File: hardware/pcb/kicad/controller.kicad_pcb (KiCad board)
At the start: 6 copper layers, 160 x 130 mm, 29 parts, among them J1 48V_INPUT_10A, J10 ESTOP_RED_KEYED_DUAL_CHANNEL, J11 SAFETY_GATE_OUTPUT, J2 12V_OUTPUT_16A, J3 JETSON_DEVKIT_12V_5A, J4 JETSON_MCU_BACKPLANE, J5 CAN_A, J6 CAN_B, U1 LM5069_HOTSWAP, U2 DCM3623_48V_12V_240W, U3 JETSON_12V_EFUSE_5A, U4 BUCK_12V_3V3_5A, U5 CH32V307_CARRIER, U6 ISO1042DW, U7 3V3_5V_ISOLATED_DC_DC, U8 DUAL_CHANNEL_SAFETY_GATE_CARR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

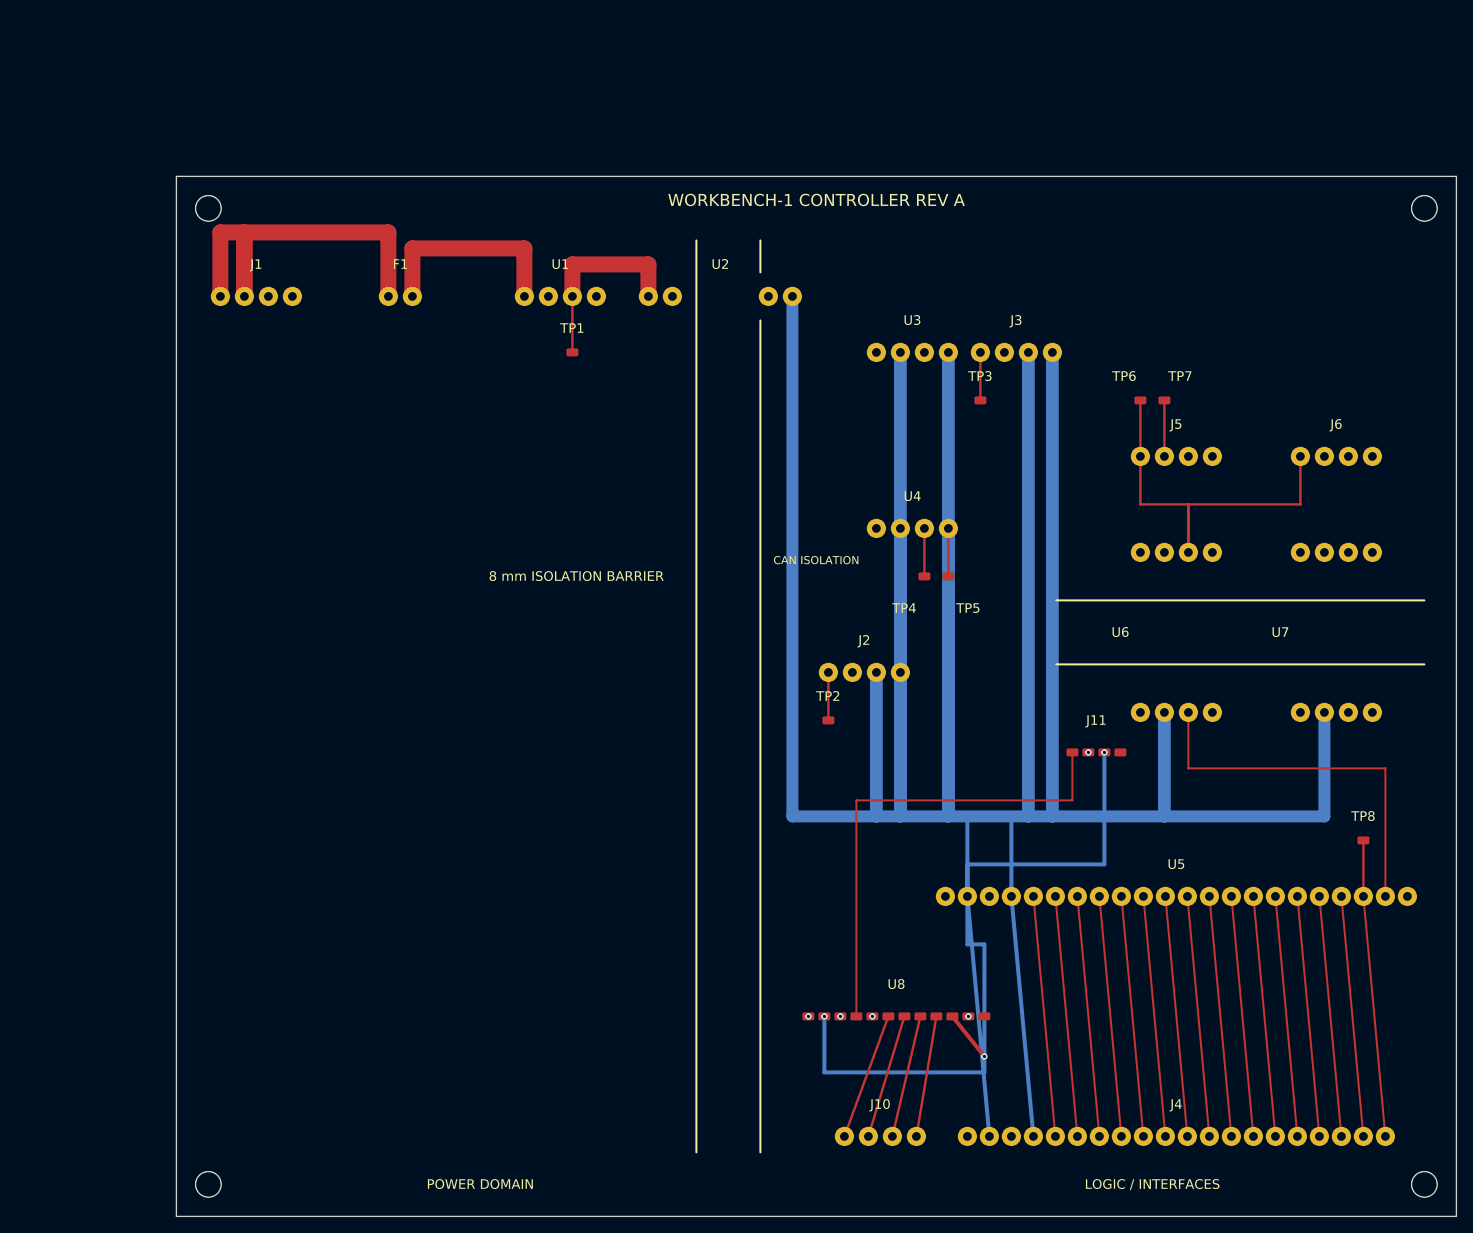
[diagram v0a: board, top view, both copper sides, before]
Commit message: feat(hardware): integrate eight-layer chassis traction package
Add reproducible eight-layer controller schematic/layout and fabrication outputs, plus fail-closed traction childboard, wheel, battery, and chassis envelopes. Keep motor, AVL, safety, supplier, and physical validation gates blocked until external evidence is attached.
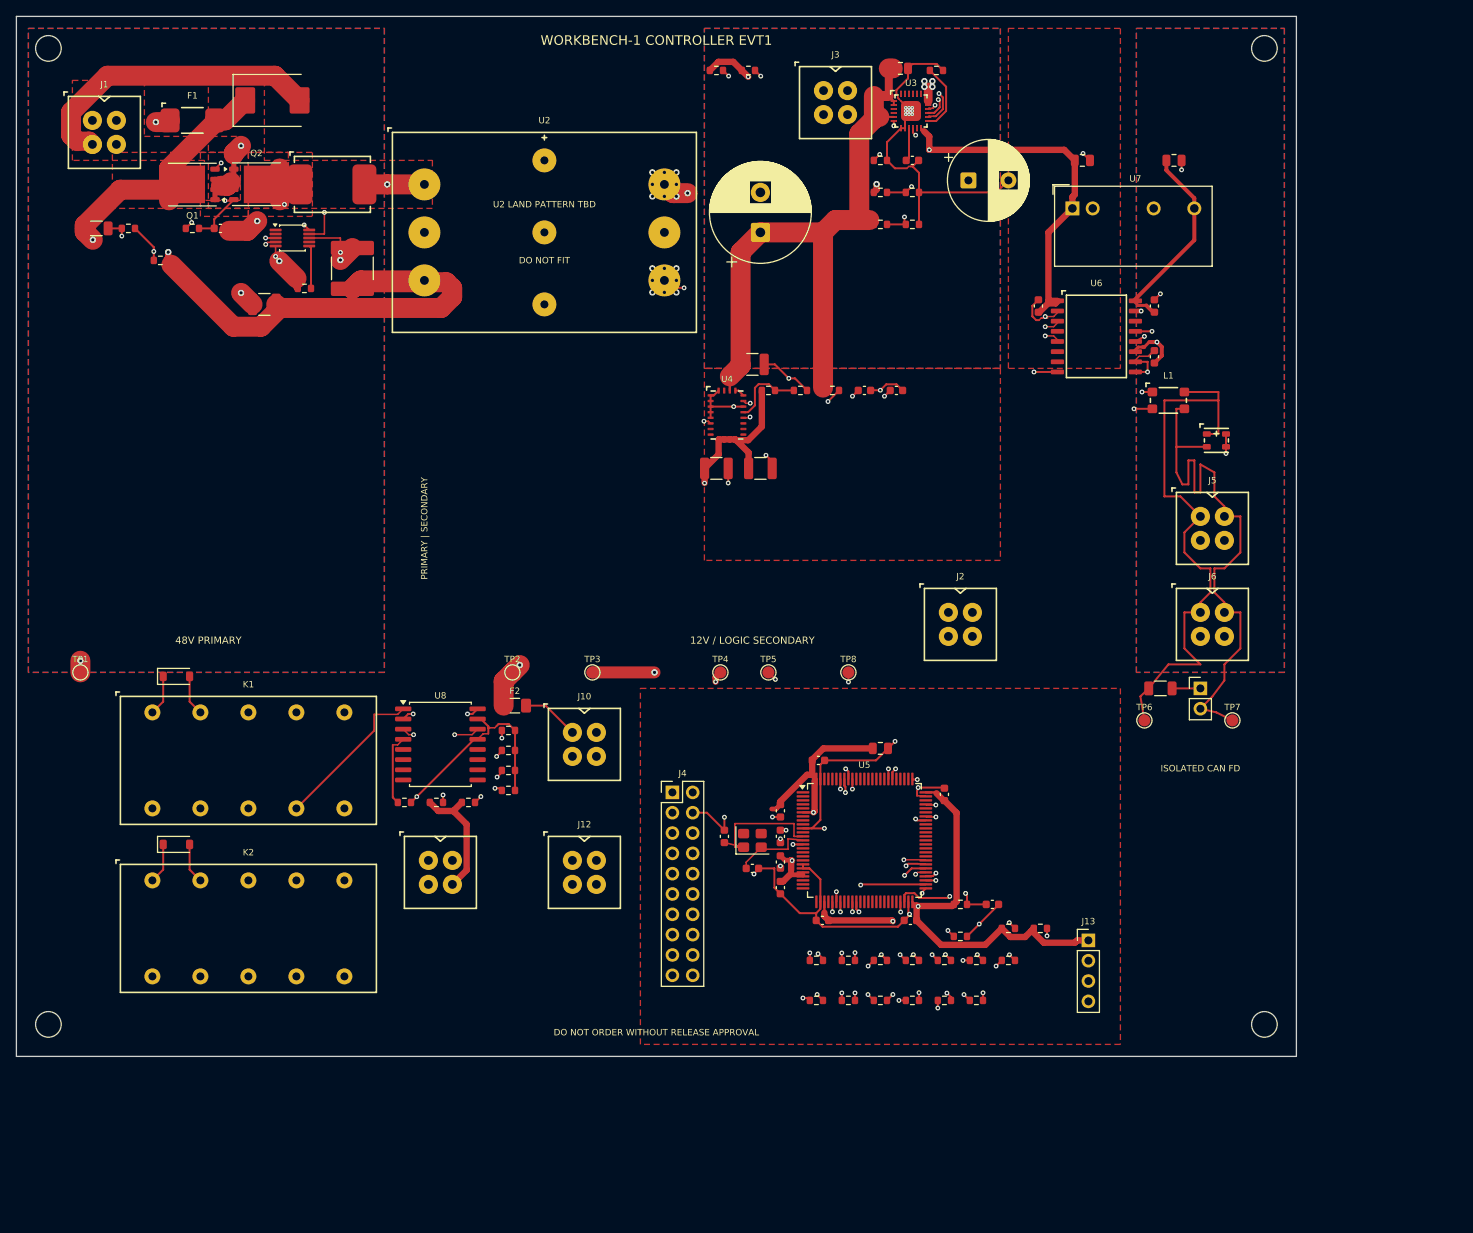
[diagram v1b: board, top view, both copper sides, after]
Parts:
- added C1: 1uF 100V, C_1210_3225Metric, F.Cu at (31.0, 36.0)
- added C10: 100nF, C_0603_1608Metric, F.Cu at (95.5, 102.5)
- added C11: 100nF, C_0603_1608Metric, F.Cu at (95.5, 105.7)
- added C12: 100nF, C_0603_1608Metric, F.Cu at (95.5, 108.9)
- added C13: 100nF, C_0603_1608Metric, F.Cu at (100.8, 113.0)
- added C14: 100nF, C_0603_1608Metric, F.Cu at (111.8, 113.0)
- added C15: 100nF, C_0603_1608Metric, F.Cu at (116.0, 97.2)
- added C16: 100nF, C_0603_1608Metric, F.Cu at (100.2, 93.0)
- added C17: 4.7uF, C_0805_2012Metric, F.Cu at (108.0, 91.5)
- added C18: 100nF, C_0603_1608Metric, F.Cu at (112.0, 18.0)
- added C19: 100nF, C_0603_1608Metric, F.Cu at (122.0, 111.0)
- added C2: 10uF 100V, C_2220_5750Metric, F.Cu at (42.0, 31.5)
- added C20: 1uF 10V, C_0603_1608Metric, F.Cu at (110.0, 46.8)
- added C3: 470uF 25V, CP_Radial_D12.5mm_P5.00mm, F.Cu at (93.0, 27.0)
- added C4: 1uF 25V, C_0805_2012Metric, F.Cu at (110.5, 6.50)
- added C40: 100nF, C_0603_1608Metric, F.Cu at (127.8, 36.2)
- added C41: 100nF, C_0603_1608Metric, F.Cu at (142.2, 36.2)
- added C42: 4.7uF, C_0805_2012Metric, F.Cu at (133.2, 18.0)
- added C43: 4.7uF, C_0805_2012Metric, F.Cu at (144.7, 18.0)
- added C44: 100nF, C_0603_1608Metric, F.Cu at (142.2, 42.5)
- added C5: 220uF 25V, CP_Radial_D10.0mm_P5.00mm, F.Cu at (119.0, 20.5)
- added C6: 22uF 25V, C_1210_3225Metric, F.Cu at (92.0, 43.5)
- added C7: 47uF 10V, C_1210_3225Metric, F.Cu at (87.5, 56.5)
- added C8: 47uF 10V, C_1210_3225Metric, F.Cu at (93.0, 56.5)
- added C9: 100nF, C_0603_1608Metric, F.Cu at (95.5, 99.3)
- added CG1: 4.7nF 100V, C_0603_1608Metric, F.Cu at (25.5, 26.5)
- added CSS4: 22nF, C_0603_1608Metric, F.Cu at (106.0, 46.8)
- added CY1: 18pF, C_0603_1608Metric, F.Cu at (88.5, 102.5)
- added CY2: 18pF, C_0603_1608Metric, F.Cu at (92.0, 106.5)
- added D1: SMCJ58A, D_SMC, F.Cu at (32.0, 10.5)
- added D2: CAN FD TVS, CAN_TVS, F.Cu at (150.0, 53.0)
- added D3: FLYBACK, D_SOD-123, F.Cu at (20.0, 82.5)
- added D4: FLYBACK, D_SOD-123, F.Cu at (20.0, 103.5)
- added F2: PTC 0.25A, Fuse_1206_3216Metric, F.Cu at (62.3, 86.2)
- added J12: DUAL MANUAL RESET, MicroFit_2x2, F.Cu at (71.0, 107.0)
- added J13: WCH DEBUG, PinHeader_1x04_P2.54mm_Vertical, F.Cu at (134.0, 115.5)
- added JP1: CAN TERM, PinHeader_1x02_P2.54mm_Vertical, F.Cu at (148.0, 84.0)
- added K1: FORCE-GUIDED 12V A, Panasonic_SFM4, F.Cu at (29.0, 93.0)
- added K2: FORCE-GUIDED 12V B, Panasonic_SFM4, F.Cu at (29.0, 114.0)
- added L1: 100R@100MHz, ACT45B, F.Cu at (144.0, 48.0)
- added Q1: 150V N-MOS, Infineon_PG-TDSON-8_6.15x5.15mm, F.Cu at (22.0, 21.0)
- added Q2: 150V N-MOS, Infineon_PG-TDSON-8_6.15x5.15mm, F.Cu at (30.0, 21.0)
- added R30: 33R, R_0603_1608Metric, F.Cu at (100.0, 118.0)
- added R31: 33R, R_0603_1608Metric, F.Cu at (104.0, 118.0)
- added R32: 33R, R_0603_1608Metric, F.Cu at (108.0, 118.0)
- added R33: 33R, R_0603_1608Metric, F.Cu at (112.0, 118.0)
- added R34: 33R, R_0603_1608Metric, F.Cu at (116.0, 118.0)
- added R35: 33R, R_0603_1608Metric, F.Cu at (120.0, 118.0)
- added R36: 33R, R_0603_1608Metric, F.Cu at (124.0, 118.0)
- added R37: 33R, R_0603_1608Metric, F.Cu at (100.0, 123.0)
- added R38: 33R, R_0603_1608Metric, F.Cu at (104.0, 123.0)
- added R39: 33R, R_0603_1608Metric, F.Cu at (108.0, 123.0)
- added R40: 33R, R_0603_1608Metric, F.Cu at (112.0, 123.0)
- added R41: 33R, R_0603_1608Metric, F.Cu at (116.0, 123.0)
- added R42: 33R, R_0603_1608Metric, F.Cu at (120.0, 123.0)
- added R43: 100k, R_0603_1608Metric, F.Cu at (118.0, 115.0)
- added R44: 100k, R_0603_1608Metric, F.Cu at (61.5, 91.8)
- added R45: 100k, R_0603_1608Metric, F.Cu at (61.5, 94.3)
- added R46: 100k, R_0603_1608Metric, F.Cu at (102.0, 46.8)
- added R47: 10k, R_0603_1608Metric, F.Cu at (91.5, 6.75)
- added R48: 3.00k 1%, R_0603_1608Metric, F.Cu at (108.0, 18.0)
- added R49: 10k, R_0603_1608Metric, F.Cu at (52.5, 98.3)
- added R50: 10k, R_0603_1608Metric, F.Cu at (56.5, 98.3)
- added R51: 10k, R_0603_1608Metric, F.Cu at (115.0, 6.75)
- added R52: 4.7k, R_0603_1608Metric, F.Cu at (61.5, 96.8)
- added R53: 4.7k, R_0603_1608Metric, F.Cu at (48.5, 98.3)
- added R54: 10k, R_0603_1608Metric, F.Cu at (118.0, 111.0)
- added R55: 4.7k, R_0603_1608Metric, F.Cu at (124.0, 114.0)
- added R56: 4.7k, R_0603_1608Metric, F.Cu at (128.0, 114.0)
- added R57: 100k, R_0603_1608Metric, F.Cu at (61.5, 89.3)
- added R58: 120R 1%, R_1206_3216Metric, F.Cu at (143.0, 84.0)
- added R59: 73.2k 1%, R_0603_1608Metric, F.Cu at (108.0, 26.0)
- added R60: 10.0k 1%, R_0603_1608Metric, F.Cu at (112.0, 26.0)
- added RFB1: 45.0k 1%, R_0603_1608Metric, F.Cu at (94.0, 46.8)
- added RFB2: 10.0k 1%, R_0603_1608Metric, F.Cu at (98.0, 46.8)
- added RG1: 22k, R_0603_1608Metric, F.Cu at (22.0, 26.5)
- added RPG1: 453k 1%, R_0603_1608Metric, F.Cu at (108.0, 22.0)
- added RPG2: 56.0k 1%, R_0603_1608Metric, F.Cu at (112.0, 22.0)
- added RPG3: 10k, R_0603_1608Metric, F.Cu at (87.5, 6.75)
- added RS1: 6mR 3W 1%, Sense_3637, F.Cu at (39.5, 21.0)
- added RSH1: 510k, R_0603_1608Metric, F.Cu at (36.0, 34.0)
- added RUV1: 19.6M 1%, R_1206_3216Metric, F.Cu at (10.0, 26.5)
- added RUV2: 133k 1%, R_0603_1608Metric, F.Cu at (14.0, 26.5)
- added RUV3: 162k 1%, R_0603_1608Metric, F.Cu at (18.0, 30.5)
- added Y1: 8MHz, Crystal_SMD_3225-4Pin_3.2x2.5mm, F.Cu at (92.0, 103.0)
- F1: value FUSE_10A -> 10A 125V; footprint (none) -> Fuse_4510
- J1: value 48V_INPUT_10A -> 48V INPUT; footprint (none) -> MicroFit_2x2
- J10: value ESTOP_RED_KEYED_DUAL_CHANNEL -> DUAL ESTOP LOOP; footprint (none) -> MicroFit_2x2
- J11: value SAFETY_GATE_OUTPUT -> SAFETY OUTPUT; footprint (none) -> MicroFit_2x2
- J2: value 12V_OUTPUT_16A -> 12V MOTOR AUX; footprint (none) -> MicroFit_2x2
- J3: value JETSON_DEVKIT_12V_5A -> JETSON DEVKIT 12V; footprint (none) -> MicroFit_2x2
- J4: value JETSON_MCU_BACKPLANE -> JETSON MCU BACKPLANE; footprint (none) -> PinHeader_2x10_P2.54mm_Vertical
- J5: value CAN_A -> CAN A; footprint (none) -> MicroFit_2x2
- J6: value CAN_B -> CAN B; footprint (none) -> MicroFit_2x2
- TP1, TP2, TP3, TP4, TP5, TP6, TP7, TP8: footprint (none) -> TestPoint_Pad_D1.5mm
- U1: value LM5069_HOTSWAP -> LTC4368HMS-2; footprint (none) -> MSOP-10_3x3mm_P0.5mm
- U2: value DCM3623_48V_12V_240W -> ISOLATED 48V-12V 240W (TBD); footprint (none) -> Isolated_48V_12V_240W_TBD
- U3: value JETSON_12V_EFUSE_5A -> TPS26633RGE; footprint (none) -> TPS26633_RGE24
- U4: value BUCK_12V_3V3_5A -> RPL-5.0 3V3/5A; footprint (none) -> RPL-5.0_QFN24
- U5: value CH32V307_CARRIER -> CH32V307VCT6; footprint (none) -> LQFP-100_14x14mm_P0.5mm
- U6: footprint (none) -> ISO1042_DW16_HV
- U7: value 3V3_5V_ISOLATED_DC_DC -> 3V3-5V ISO 1W; footprint (none) -> Converter_DCDC_muRata_MEJ1SxxxxSC_THT
- U8: value DUAL_CHANNEL_SAFETY_GATE_CARRIER -> ESTOP DIAGNOSTIC OPTO; footprint (none) -> SOIC-16W_7.5x10.3mm_P1.27mm
- moved J11 83.4 mm to (53.0, 107.0)
- moved J4 76.3 mm to (82.0, 97.0)
- moved TP1 73.4 mm to (8.00, 82.0)
- moved TP8 67.7 mm to (104.0, 82.0)
- moved U8 66.4 mm to (53.0, 91.0)
- moved U7 62.4 mm to (132.0, 24.0)
- moved J10 61.4 mm to (71.0, 91.0)
- moved TP3 59.2 mm to (72.0, 82.0)
- moved TP7 40.9 mm to (152.0, 88.0)
- moved TP6 40.0 mm to (141.0, 88.0)
- moved TP2 40.0 mm to (62.0, 82.0)
- moved U5 39.6 mm to (106.0, 103.0)
- moved J3 38.6 mm to (102.4, 10.8)
- moved U6 38.3 mm to (135.0, 40.0)
- moved U1 34.3 mm to (34.5, 27.7)
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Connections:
- J10 pad 1: ESTOP_CH_A_OUT -> ESTOP_12V
- J10 pad 3: ESTOP_CH_B_OUT -> ESTOP_12V
- J11 pad 4: (no net) -> 3V3_LOGIC
- J4 pad 8: MOTOR_ENABLE_REQ -> JETSON_ENABLE_REQ
- U1 pad 1: VBAT_FUSED -> GND_PWR
- U1 pad 3: VBAT_PROTECTED -> OV_SET
- U1 pad 4: GND_PWR -> UV_SET
- U2 pad 3: 12V_ISO -> (no net)
- U2 pad 4: GND -> 12V_ISO
- U3 pad 2: GND -> 12V_ISO
- U3 pad 3: JETSON_12V -> (no net)
- U3 pad 4: GND -> (no net)
- U4 pad 1: 12V_ISO -> GND
- U4 pad 3: 3V3_LOGIC -> GND
- U5 pad 1: 3V3_LOGIC -> (no net)
- U5 pad 10: MOTOR_CS1 -> GND
- U5 pad 11: MOTOR_CS2 -> 3V3_LOGIC
- U5 pad 12: MOTOR_CS3 -> OSC_IN
- U5 pad 13: MOTOR_CS4 -> OSC_OUT
- U5 pad 14: MOTOR_CS5 -> MCU_RESET
- U5 pad 15: I2C_SDA -> (no net)
- U5 pad 16: I2C_SCL -> (no net)
- U5 pad 17: ESTOP_SENSE -> (no net)
- U5 pad 18: UART_TX -> (no net)
- U5 pad 19: UART_RX -> GND
- U5 pad 2: GND -> (no net)
- U5 pad 20: MCU_RESET -> GND
- U5 pad 21: CAN_TX -> 3V3_LOGIC
- U5 pad 22: CAN_RX -> 3V3_LOGIC
- U5 pad 3: 3V3_LOGIC -> (no net)
- U5 pad 4: GND -> (no net)
- U5 pad 5: SPI_SCLK -> (no net)
- U5 pad 6: SPI_MOSI -> 3V3_LOGIC
- U5 pad 7: SPI_MISO -> (no net)
- U5 pad 8: MOTOR_ENABLE_REQ -> (no net)
- U5 pad 9: MOTOR_CS0 -> (no net)
- U6 pad 1: 5V_CAN_ISO -> 3V3_LOGIC
- U6 pad 2: GND_CAN_ISO -> GND
- U6 pad 3: CANH -> CAN_TX
- U6 pad 4: CANL -> (no net)
- U6 pad 5: 3V3_LOGIC -> CAN_RX
- U6 pad 6: GND -> (no net)
- U6 pad 7: CAN_TX -> (no net)
- U6 pad 8: CAN_RX -> GND
- U7 pad 1: 5V_CAN_ISO -> 3V3_LOGIC
- U7 pad 2: GND_CAN_ISO -> GND
- U7 pad 5: 3V3_LOGIC -> GND_CAN_ISO
- U7 pad 7: (no net) -> 5V_CAN_ISO
- U8 pad 1: 12V_ISO -> ESTOP_CH_A_RETURN
- U8 pad 10: GND -> (no net)
- U8 pad 11: 3V3_LOGIC -> (no net)
- U8 pad 2: GND -> U8_LED_A_K
- U8 pad 3: MOTOR_ENABLE_REQ -> ESTOP_CH_B_RETURN
- U8 pad 4: MOTOR_ENABLE_SAFE -> U8_LED_B_K
- U8 pad 5: ESTOP_SENSE -> (no net)
- U8 pad 6: ESTOP_CH_A_OUT -> (no net)
- U8 pad 7: ESTOP_CH_A_RETURN -> (no net)
- U8 pad 8: ESTOP_CH_B_OUT -> (no net)
- U8 pad 9: ESTOP_CH_B_RETURN -> (no net)
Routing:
- net GND: track 1029.4 -> 582.5 mm, vias 3 -> 38
- net 3V3_LOGIC: track 213.9 -> 487.8 mm, vias 1 -> 9
- net RELAY_B_NC: track 0.00 -> 113.5 mm, vias 0 -> 2
- net RELAY_A_NC: track 0.00 -> 107.3 mm, vias 0 -> 2
- net JETSON_12V: track 36.0 -> 141.9 mm, vias 0 -> 6
- net ESTOP_A_MON: track 0.00 -> 78.0 mm, vias 0 -> 3
- net VBAT_PROTECTED: track 24.5 -> 100.1 mm, vias 0 -> 5
- net ESTOP_B_MON: track 0.00 -> 72.2 mm, vias 0 -> 3
- net RESET_CH_B_RETURN: track 0.00 -> 70.3 mm
- net RESET_CH_A_RETURN: track 0.00 -> 68.2 mm
- net ESTOP_CH_B_RETURN: track 15.2 -> 79.1 mm, vias 0 -> 1
- net ESTOP_CH_A_RETURN: track 15.7 -> 74.1 mm
- net ESTOP_SENSE: track 170.3 -> 113.0 mm
- net VBAT_RAW: track 53.0 -> 9.88 mm, vias 0 -> 1
- net MOTOR_ENABLE_SAFE: track 60.0 -> 17.5 mm
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- added copper zone on In2.Cu, net 12V_ISO
- added copper zone on F.Cu, net 3V3_LOGIC
- added copper zone on In5.Cu, net 3V3_LOGIC
- added copper zone on In5.Cu, net 5V_CAN_ISO
- added copper zone on F.Cu, net FET_COMMON
- added copper zone on In1.Cu, net GND
- added copper zone on In4.Cu, net GND
- added copper zone on B.Cu, net GND_CAN_ISO
- added copper zone on F.Cu, net GND_CAN_ISO
- added copper zone on In1.Cu, net GND_CAN_ISO
- added copper zone on In4.Cu, net GND_CAN_ISO
- added copper zone on B.Cu, net GND_PWR
- added copper zone on F.Cu, net GND_PWR
- added copper zone on In1.Cu, net GND_PWR
- added copper zone on F.Cu, net INPUT_SENSE
- added copper zone on B.Cu, net JETSON_12V
- added copper zone on F.Cu, net JETSON_12V
- added copper zone on In3.Cu, net JETSON_12V
- added copper zone on F.Cu, net VBAT_FUSED
- added copper zone on F.Cu, net VBAT_PROTECTED
- added copper zone on F.Cu, net VBAT_RAW
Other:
- copper layers 6 -> 8
- board text added: "12V / LOGIC SECONDARY"
- board text added: "48V PRIMARY"
- board text added: "DO NOT FIT"
- board text added: "DO NOT ORDER WITHOUT RELEASE APPROVAL"
- board text added: "FAB: ENIG | THK 1.60 +/- 0.16 MM (MASK EXCL)"
- board text added: "FAB: U3 HDI 9x 0.45/0.15 FILL/CAP/PLANARIZE"
- board text added: "ISOLATED CAN FD"
- board text added: "PRIMARY | SECONDARY"
- board text added: "U2 LAND PATTERN TBD"
- board text added: "WORKBENCH-1 CONTROLLER EVT1"
- board text removed: "8 mm ISOLATION BARRIER"
- board text removed: "CAN ISOLATION"
- board text removed: "LOGIC / INTERFACES"
- board text removed: "POWER DOMAIN"
- board text removed: "WORKBENCH-1 CONTROLLER REV A"
